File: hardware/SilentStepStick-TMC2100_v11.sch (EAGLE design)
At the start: 30 parts, among them IC1 TMC2100_QFN36, X1 PASSER-07, X2 PASSER-07

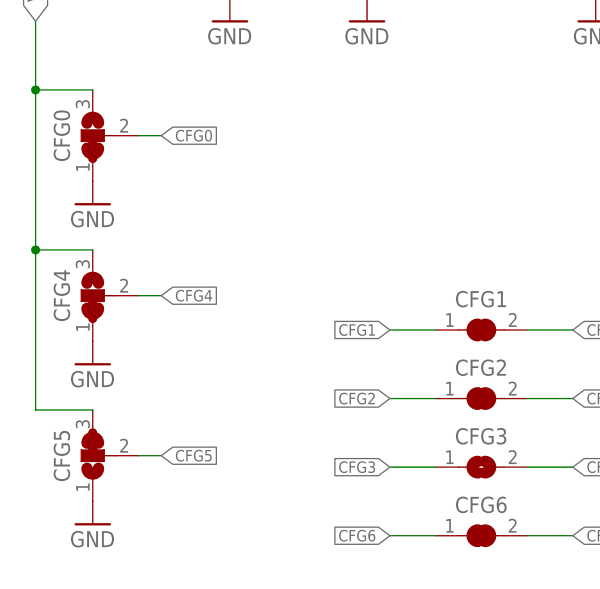
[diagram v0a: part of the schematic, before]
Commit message: updated schematics
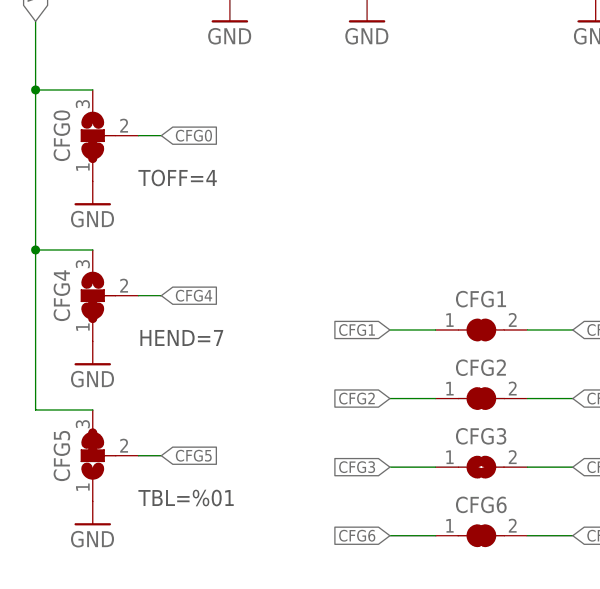
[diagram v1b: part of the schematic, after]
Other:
- note added: "HEND=7"
- note added: "TBL=%01"
- note added: "TOFF=4"
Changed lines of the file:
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@@
 <?xml version="1.0" encoding="utf-8"?>
 <!DOCTYPE eagle SYSTEM "eagle.dtd">
-<eagle version="7.5.0">
+<eagle version="7.7.0">
 <drawing>
 <settings>
@@
 <setting verticaltext="up"/>
 </settings>
-<grid distance="0.1" unitdist="inch" unit="inch" style="lines" multiple="1" display="no" altdistance="0.01" altunitdist="inch" altunit="inch"/>
+<grid distance="0.05" unitdist="inch" unit="inch" style="lines" multiple="1" display="yes" altdistance="0.025" altunitdist="inch" altunit="inch"/>
 <layers>
 <layer number="1" name="Top" color="4" fill="1" visible="no" active="no"/>
@@
 <layer number="53" name="tPadExt" color="7" fill="6" visible="no" active="no"/>
 <layer number="54" name="bPadExt" color="1" fill="3" visible="no" active="no"/>
+<layer number="90" name="Modules" color="5" fill="1" visible="yes" active="yes"/>
 <layer number="91" name="Nets" color="2" fill="1" visible="yes" active="yes"/>
 <layer number="92" name="Busses" color="1" fill="1" visible="yes" active="yes"/>
@@
 <wire x1="59.055" y1="24.13" x2="60.325" y2="24.13" width="1.016" layer="94"/>
 <wire x1="16.51" y1="50.8" x2="16.51" y2="53.34" width="1.016" layer="94"/>
+<text x="21.59" y="49.53" size="1.778" layer="97" font="vector" ratio="10" align="top-left">TOFF=4</text>
+<text x="21.59" y="31.75" size="1.778" layer="97" font="vector" ratio="10" align="top-left">HEND=7</text>
+<text x="21.59" y="13.97" size="1.778" layer="97" font="vector" ratio="10" align="top-left">TBL=%01</text>
 </plain>
 <instances>
